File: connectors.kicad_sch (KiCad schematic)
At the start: 24 parts, among them J1 Conn_01x02, J4 USB_C_Receptacle_USB2.0_14P, M1 Motor_Servo, M2 Motor_Servo, Q1 Q_NMOS, Q2 Q_NMOS, U5 LM74502

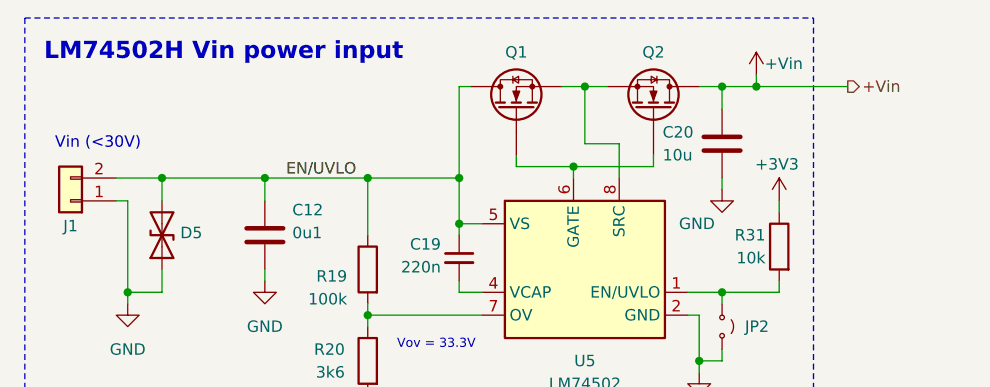
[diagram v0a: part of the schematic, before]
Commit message: schem: add test points
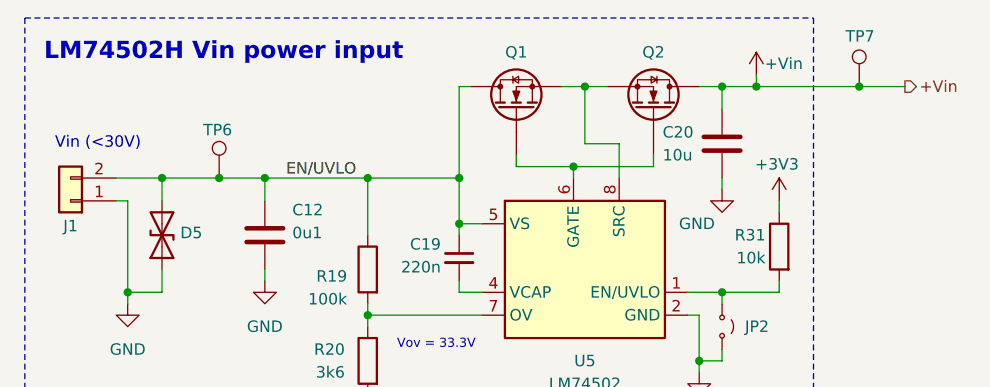
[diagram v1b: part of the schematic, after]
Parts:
- added TP6, TP7: TestPoint, symbol Connector:TestPoint
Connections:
- net +Vin: now also TP7.1
- net EN/UVLO: now also TP6.1
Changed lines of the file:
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@@
 	)
 	(junction
+		(at 240.03 85.09)
+		(diameter 0)
+		(color 0 0 0 0)
+	)
+	(junction
 		(at 93.98 147.32)
 		(diameter 0)
@@
 	)
 	(junction
+		(at 168.91 95.25)
+		(diameter 0)
+		(color 0 0 0 0)
+	)
+	(junction
 		(at 93.98 157.48)
 		(diameter 0)
@@
 	(wire
 		(pts
+			(xy 240.03 85.09) (xy 245.11 85.09)
+		)
+		(stroke
+			(width 0)
+			(type default)
+		)
+	)
+	(wire
+		(pts
 			(xy 162.56 107.95) (xy 158.75 107.95)
 		)
@@
 	(wire
 		(pts
-			(xy 162.56 95.25) (xy 173.99 95.25)
+			(xy 162.56 95.25) (xy 168.91 95.25)
 		)
 		(stroke
@@
 	(wire
 		(pts
-			(xy 228.6 85.09) (xy 238.76 85.09)
+			(xy 228.6 85.09) (xy 240.03 85.09)
 		)
 		(stroke
@@
 	(wire
 		(pts
+			(xy 168.91 95.25) (xy 173.99 95.25)
+		)
+		(stroke
+			(width 0)
+			(type default)
+		)
+	)
+	(wire
+		(pts
 			(xy 90.17 106.68) (xy 87.63 106.68)
 		)
@@
 	(hierarchical_label "+Vin"
 		(shape output)
-		(at 238.76 85.09 0)
+		(at 245.11 85.09 0)
 		(effects
 			(font
@@
 	)
 	(symbol
+		(lib_id "Connector:TestPoint")
+		(at 240.03 85.09 0)
+		(unit 1)
+		(exclude_from_sim no)
+		(in_bom yes)
+		(on_board yes)
+		(dnp no)
+		(property "Reference" "TP7"
+			(at 238.506 79.502 0)
+			(effects
+				(font
+					(size 1.27 1.27)
+				)
+				(justify left)
+			)
+		)
+		(property "Value" "TestPoint"
+			(at 242.57 83.0579 0)
+			(effects
+				(font
+					(size 1.27 1.27)
+				)
+				(justify left)
+				(hide yes)
+			)
+		)
+		(property "Footprint" ""
+			(at 245.11 85.09 0)
+			(effects
+				(font
+					(size 1.27 1.27)
+				)
+				(hide yes)
+			)
+		)
+		(property "Datasheet" "~"
+			(at 245.11 85.09 0)
+			(effects
+				(font
+					(size 1.27 1.27)
+				)
+				(hide yes)
+			)
+		)
+		(property "Description" "test point"
+			(at 240.03 85.09 0)
+			(effects
+				(font
+					(size 1.27 1.27)
+				)
+				(hide yes)
+			)
+		)
+		(pin "1"
+		)
+		(instances
+			(project "motor-power-poc"
+				(path "/a1dc4c9e-7b20-4b66-a693-9133bc644c6b/dba74ea3-505d-49e4-ba26-48f567962081"
+					(reference "TP7")
+					(unit 1)
+				)
+			)
+		)
+	)
+	(symbol
 		(lib_id "power:+3V3")
 		(at 231.14 97.79 0)
@@
 					(unit 1)
 				)
+			)
+		)
+	)
+	(symbol
+		(lib_id "Connector:TestPoint")
+		(at 168.91 95.25 0)
+		(unit 1)
+		(exclude_from_sim no)
+		(in_bom yes)
+		(on_board yes)
+		(dnp no)
+		(property "Reference" "TP6"
+			(at 167.132 89.916 0)
+			(effects
+				(font
+					(size 1.27 1.27)
+				)
+				(justify left)
+			)
+		)
+		(property "Value" "TestPoint"
+			(at 171.45 93.2179 0)
+			(effects
+				(font
+					(size 1.27 1.27)
+				)
+				(justify left)
+				(hide yes)
+			)
+		)
+		(property "Footprint" ""
+			(at 173.99 95.25 0)
+			(effects
+				(font
+					(size 1.27 1.27)
+				)
+				(hide yes)
+			)
+		)
+		(property "Datasheet" "~"
+			(at 173.99 95.25 0)
+			(effects
+				(font
+					(size 1.27 1.27)
+				)
+				(hide yes)
+			)
+		)
+		(property "Description" "test point"
+			(at 168.91 95.25 0)
+			(effects
+				(font
+					(size 1.27 1.27)
+				)
+				(hide yes)
+			)
+		)
+		(pin "1"
+		)
+		(instances
+			(project "motor-power-poc"
+				(path "/a1dc4c9e-7b20-4b66-a693-9133bc644c6b/dba74ea3-505d-49e4-ba26-48f567962081"
+					(reference "TP6")
+					(unit 1)
+				)

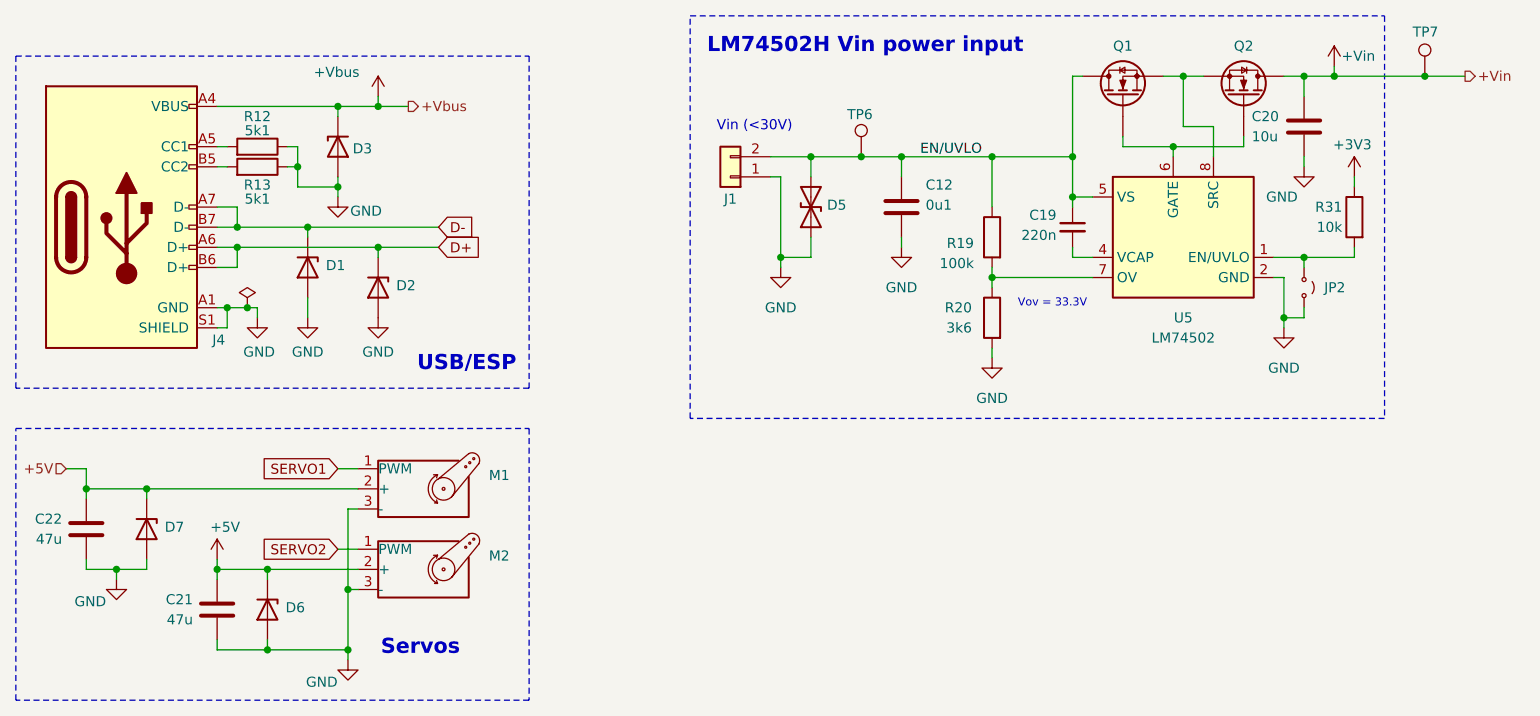
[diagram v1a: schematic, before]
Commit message: schem: renumber
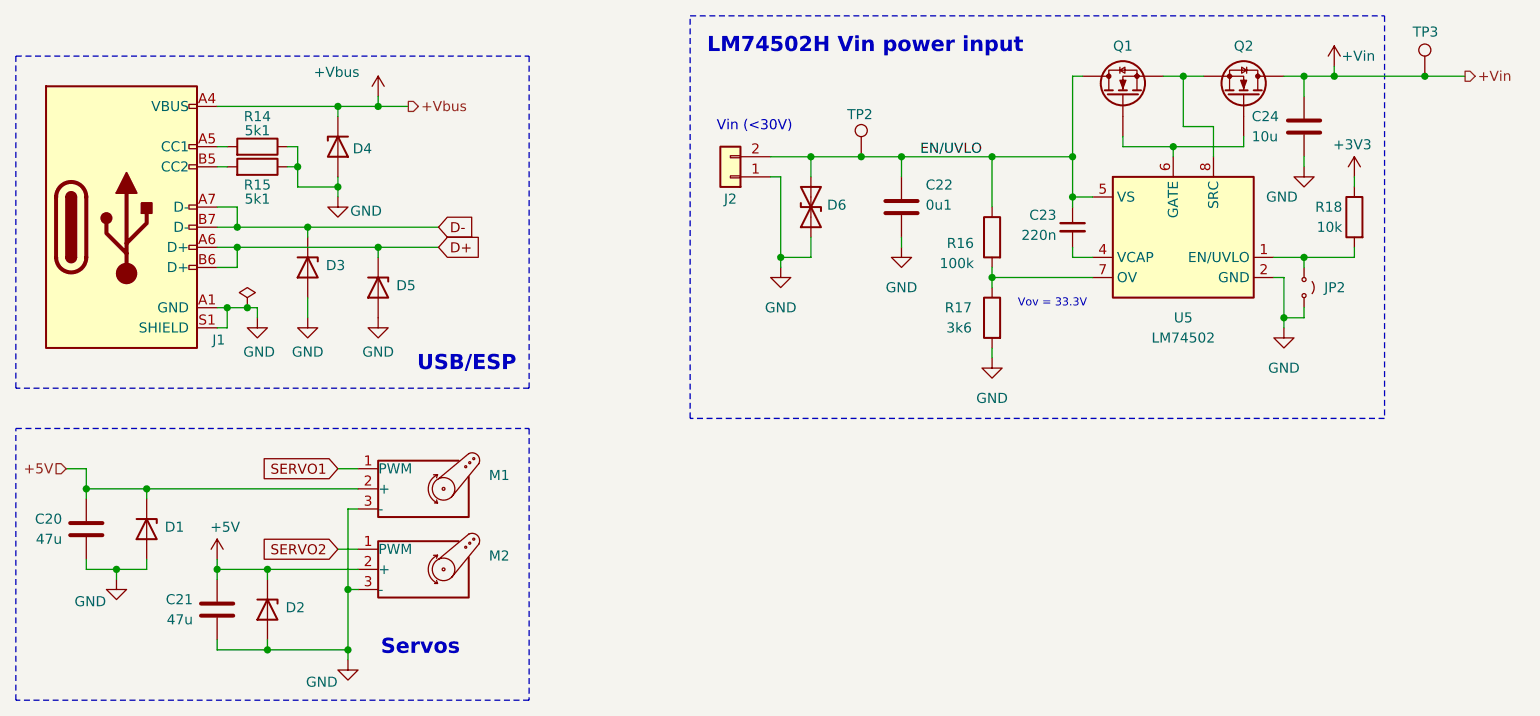
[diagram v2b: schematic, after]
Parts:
- renumbered C22 to C20, C12 to C22, C19 to C23, C20 to C24, D7 to D1, D6 to D2, D1 to D3, D3 to D4, D2 to D5, D5 to D6, J4 to J1, J1 to J2, R12 to R14, R13 to R15, R19 to R16, R20 to R17, R31 to R18, TP6 to TP2, TP7 to TP3

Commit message: schem: run and fix ERC
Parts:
- U5: footprint GLCS:SOT-23-8 -> GLCS:SOT-23-THIN-8
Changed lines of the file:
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@@
 	)
 	(junction
+		(at 232.41 85.09)
+		(diameter 0)
+		(color 0 0 0 0)
+	)
+	(junction
 		(at 240.03 85.09)
 		(diameter 0)
@@
 		(color 0 0 0 0)
 	)
+	(junction
+		(at 165.1 95.25)
+		(diameter 0)
+		(color 0 0 0 0)
+	)
 	(wire
 		(pts
@@
 	(wire
 		(pts
+			(xy 232.41 85.09) (xy 240.03 85.09)
+		)
+		(stroke
+			(width 0)
+			(type default)
+		)
+	)
+	(wire
+		(pts
 			(xy 90.17 106.68) (xy 107.95 106.68)
 		)
@@
 	(wire
 		(pts
+			(xy 165.1 95.25) (xy 168.91 95.25)
+		)
+		(stroke
+			(width 0)
+			(type default)
+		)
+	)
+	(wire
+		(pts
 			(xy 102.87 100.33) (xy 102.87 99.06)
 		)
@@
 	(wire
 		(pts
-			(xy 162.56 95.25) (xy 168.91 95.25)
+			(xy 162.56 95.25) (xy 165.1 95.25)
 		)
 		(stroke
@@
 	(wire
 		(pts
-			(xy 228.6 85.09) (xy 240.03 85.09)
+			(xy 228.6 85.09) (xy 232.41 85.09)
 		)
 		(stroke
@@
 	)
 	(symbol
+		(lib_id "power:PWR_FLAG")
+		(at 232.41 85.09 180)
+		(unit 1)
+		(exclude_from_sim no)
+		(in_bom yes)
+		(on_board yes)
+		(dnp no)
+		(fields_autoplaced yes)
+		(property "Reference" "#FLG07"
+			(at 232.41 86.995 0)
+			(effects
+				(font
+					(size 1.27 1.27)
+				)
+				(hide yes)
+			)
+		)
+		(property "Value" "PWR_FLAG"
+			(at 232.41 90.17 0)
+			(effects
+				(font
+					(size 1.27 1.27)
+				)
+				(hide yes)
+			)
+		)
+		(property "Footprint" ""
+			(at 232.41 85.09 0)
+			(effects
+				(font
+					(size 1.27 1.27)
+				)
+				(hide yes)
+			)
+		)
+		(property "Datasheet" "~"
+			(at 232.41 85.09 0)
+			(effects
+				(font
+					(size 1.27 1.27)
+				)
+				(hide yes)
+			)
+		)
+		(property "Description" "Special symbol for telling ERC where power comes from"
+			(at 232.41 85.09 0)
+			(effects
+				(font
+					(size 1.27 1.27)
+				)
+				(hide yes)
+			)
+		)
+		(pin "1"
+		)
+		(instances
+			(project "motor-power-poc"
+				(path "/a1dc4c9e-7b20-4b66-a693-9133bc644c6b/dba74ea3-505d-49e4-ba26-48f567962081"
+					(reference "#FLG07")
+					(unit 1)
+				)
+			)
+		)
+	)
+	(symbol
 		(lib_id "Device:D_TVS")
 		(at 162.56 101.6 90)
@@
 	)
 	(symbol
+		(lib_id "power:PWR_FLAG")
+		(at 165.1 95.25 0)
+		(unit 1)
+		(exclude_from_sim no)
+		(in_bom yes)
+		(on_board yes)
+		(dnp no)
+		(fields_autoplaced yes)
+		(property "Reference" "#FLG06"
+			(at 165.1 93.345 0)
+			(effects
+				(font
+					(size 1.27 1.27)
+				)
+				(hide yes)
+			)
+		)
+		(property "Value" "PWR_FLAG"
+			(at 165.1 90.17 0)
+			(effects
+				(font
+					(size 1.27 1.27)
+				)
+				(hide yes)
+			)
+		)
+		(property "Footprint" ""
+			(at 165.1 95.25 0)
+			(effects
+				(font
+					(size 1.27 1.27)
+				)
+				(hide yes)
+			)
+		)
+		(property "Datasheet" "~"
+			(at 165.1 95.25 0)
+			(effects
+				(font
+					(size 1.27 1.27)
+				)
+				(hide yes)
+			)
+		)
+		(property "Description" "Special symbol for telling ERC where power comes from"
+			(at 165.1 95.25 0)
+			(effects
+				(font
+					(size 1.27 1.27)
+				)
+				(hide yes)
+			)
+		)
+		(pin "1"
+		)
+		(instances
+			(project "motor-power-poc"
+				(path "/a1dc4c9e-7b20-4b66-a693-9133bc644c6b/dba74ea3-505d-49e4-ba26-48f567962081"
+					(reference "#FLG06")
+					(unit 1)
+				)
+			)
+		)
+	)
+	(symbol
 		(lib_id "power:GND")
 		(at 102.87 100.33 0)
@@
 			)
 		)
-		(property "Footprint" "GLCS:SOT-23-8"
+		(property "Footprint" "GLCS:SOT-23-THIN-8"
 			(at 200.025 114.3 0)
 			(effects

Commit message: schem: add title
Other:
- company: (none) -> Rémi Ait-Younes
- title: (none) -> Motor Power POC
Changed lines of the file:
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@@
 	(generator_version "9.0")
 	(paper "A4")
+	(title_block
+		(title "Motor Power POC")
+		(date "2025-11-30")
+		(rev "01")
+		(company "Rémi Ait-Younes")
+	)
 	(rectangle
 		(start 147.32 77.47)

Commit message: schem: assign footprints
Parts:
- C20, C21: footprint (none) -> Capacitor_SMD:C_1206_3216Metric
- C22, C23: footprint (none) -> Capacitor_SMD:C_0402_1005Metric
- C24: footprint (none) -> Capacitor_SMD:C_0805_2012Metric
- D1, D2, D3, D5: footprint Pers:Diode_DFN1006 -> GLCS:Diode_DFN1006; symbol Pers:H5VU10U -> GLCS:H5VU10U
- D4: footprint Diode_SMD:D_SMB -> GLCS:Diode_DFN1006; symbol Pers:H5VU10U -> GLCS:H5VU10U
- D6: footprint (none) -> Diode_SMD:D_SMB; Basic (none) -> E; JLCPCB Part # (none) -> C2925441; Manufacturer (none) -> Liown; Manufacturer Part Number (none) -> SMBJ30CA
- JP2: footprint (none) -> Connector_PinHeader_2.54mm:PinHeader_1x02_P2.54mm_Vertical
- M1, M2: footprint (none) -> Connector_PinHeader_2.54mm:PinHeader_1x03_P2.54mm_Vertical
- Q1, Q2: footprint (none) -> Package_SO:Vishay_PowerPAK_1212-8_Single
- R16, R18: footprint (none) -> Resistor_SMD:R_0402_1005Metric
- R17: footprint (none) -> Resistor_SMD:R_0603_1608Metric
- TP2, TP3: footprint (none) -> GLCS:TestPoint_Keystone_5015_Micro_Mini
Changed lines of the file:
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@@
 			)
 		)
-		(property "Footprint" ""
+		(property "Footprint" "Diode_SMD:D_SMB"
 			(at 162.56 101.6 0)
 			(effects
@@
 		(property "Description" "Bidirectional transient-voltage-suppression diode"
 			(at 162.56 101.6 0)
+			(effects
+				(font
+					(size 1.27 1.27)
+				)
+				(hide yes)
+			)
+		)
+		(property "Basic" "E"
+			(at 162.56 101.6 90)
+			(effects
+				(font
+					(size 1.27 1.27)
+				)
+				(hide yes)
+			)
+		)
+		(property "JLCPCB Part #" "C2925441"
+			(at 162.56 101.6 90)
+			(effects
+				(font
+					(size 1.27 1.27)
+				)
+				(hide yes)
+			)
+		)
+		(property "Manufacturer" "Liown"
+			(at 162.56 101.6 90)
+			(effects
+				(font
+					(size 1.27 1.27)
+				)
+				(hide yes)
+			)
+		)
+		(property "Manufacturer Part Number" "SMBJ30CA"
+			(at 162.56 101.6 90)
 			(effects
 				(font
@@
 			)
 		)
-		(property "Footprint" ""
+		(property "Footprint" "Capacitor_SMD:C_1206_3216Metric"
 			(at 70.1548 146.05 0)
 			(effects
@@
 	)
 	(symbol
-		(lib_id "Pers:H5VU10U")
+		(lib_id "GLCS:H5VU10U")
 		(at 107.95 111.76 270)
 		(unit 1)
@@
 			)
 		)
-		(property "Footprint" "Pers:Diode_DFN1006"
+		(property "Footprint" "GLCS:Diode_DFN1006"
 			(at 103.505 111.76 0)
 			(effects
@@
 	)
 	(symbol
-		(lib_id "Pers:H5VU10U")
+		(lib_id "GLCS:H5VU10U")
 		(at 99.06 109.22 270)
 		(unit 1)
@@
 			)
 		)
-		(property "Footprint" "Pers:Diode_DFN1006"
+		(property "Footprint" "GLCS:Diode_DFN1006"
 			(at 94.615 109.22 0)
 			(effects
@@
 			)
 		)
-		(property "Footprint" ""
+		(property "Footprint" "Connector_PinHeader_2.54mm:PinHeader_1x02_P2.54mm_Vertical"
 			(at 224.79 111.76 0)
 			(effects
@@
 			)
 		)
-		(property "Footprint" ""
+		(property "Footprint" "Package_SO:Vishay_PowerPAK_1212-8_Single"
 			(at 219.71 82.55 0)
 			(effects
@@
 	)
 	(symbol
-		(lib_id "Pers:H5VU10U")
+		(lib_id "GLCS:H5VU10U")
 		(at 78.74 142.24 270)
 		(unit 1)
@@
 			)
 		)
-		(property "Footprint" "Pers:Diode_DFN1006"
+		(property "Footprint" "GLCS:Diode_DFN1006"
 			(at 74.295 142.24 0)
 			(effects
@@
 			)
 		)
-		(property "Footprint" ""
+		(property "Footprint" "Capacitor_SMD:C_0402_1005Metric"
 			(at 195.58 104.14 0)
 			(effects
@@
 			)
 		)
-		(property "Footprint" ""
+		(property "Footprint" "Capacitor_SMD:C_0402_1005Metric"
 			(at 173.0248 105.41 0)
 			(effects
@@
 			)
 		)
-		(property "Footprint" ""
+		(property "Footprint" "GLCS:TestPoint_Keystone_5015_Micro_Mini"
 			(at 245.11 85.09 0)
 			(effects
@@
 			)
 		)
-		(property "Footprint" ""
+		(property "Footprint" "GLCS:TestPoint_Keystone_5015_Micro_Mini"
 			(at 173.99 95.25 0)
 			(effects
@@
 			)
 		)
-		(property "Footprint" ""
+		(property "Footprint" "Capacitor_SMD:C_0805_2012Metric"
 			(at 223.8248 95.25 0)
 			(effects
@@
 	)
 	(symbol
-		(lib_id "Pers:H5VU10U")
+		(lib_id "GLCS:H5VU10U")
 		(at 102.87 93.98 90)
 		(mirror x)
@@
 			)
 		)
-		(property "Footprint" "Diode_SMD:D_SMB"
+		(property "Footprint" "GLCS:Diode_DFN1006"
 			(at 107.315 93.98 0)
 			(effects
@@
 			)
 		)
-		(property "Datasheet" "https://www.lcsc.com/datasheet/C78395.pdf"
+		(property "Datasheet" "https://datasheet.lcsc.com/lcsc/2504101957_hongjiacheng-H5VU10U_C22395519.pdf"
 			(at 102.87 93.98 0)
 			(effects
@@
 			)
 		)
-		(property "Description" "10.5V 1uA 5.8V 58.1A 6.45V 600W Bidirectional TVS SMB(DO-214AA) ESD and Surge Protection (TVS/ESD) ROHS"
+		(property "Description" "-55℃~+155℃ 0.8pF 16V 200nA 55W@8/20us 5A@8/20us 5V 6V ESD IEC 61000-4-2 Unidirectional DFN1006-2L ESD and Surge Protection (TVS/ESD) ROHS"
 			(at 102.87 93.98 0)
 			(effects
@@
 			)
 		)
-		(property "Footprint" ""
+		(property "Footprint" "Resistor_SMD:R_0603_1608Metric"
 			(at 187.198 115.57 90)
 			(effects
@@
 			)
 		)
-		(property "Footprint" ""
+		(property "Footprint" "Capacitor_SMD:C_1206_3216Metric"
 			(at 86.6648 156.21 0)
 			(effects
@@
 	)
 	(symbol
-		(lib_id "Pers:H5VU10U")
+		(lib_id "GLCS:H5VU10U")
 		(at 93.98 152.4 270)
 		(unit 1)
@@
 			)
 		)
-		(property "Footprint" "Pers:Diode_DFN1006"
+		(property "Footprint" "GLCS:Diode_DFN1006"
 			(at 89.535 152.4 0)
 			(effects
@@
 			)
 		)
-		(property "Footprint" ""
+		(property "Footprint" "Connector_PinHeader_2.54mm:PinHeader_1x03_P2.54mm_Vertical"
 			(at 113.03 152.146 0)
 			(effects
@@
 			)
 		)
-		(property "Footprint" ""
+		(property "Footprint" "Connector_PinHeader_2.54mm:PinHeader_1x03_P2.54mm_Vertical"
 			(at 113.03 141.986 0)
 			(effects
@@
 			)
 		)
-		(property "Footprint" ""
+		(property "Footprint" "Resistor_SMD:R_0402_1005Metric"
 			(at 187.198 105.41 90)
 			(effects
@@
 			)
 		)
-		(property "Footprint" ""
+		(property "Footprint" "Package_SO:Vishay_PowerPAK_1212-8_Single"
 			(at 199.39 82.55 0)
 			(effects
@@
 			)
 		)
-		(property "Footprint" ""
+		(property "Footprint" "Resistor_SMD:R_0402_1005Metric"
 			(at 232.918 102.87 90)
 			(effects

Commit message: schem: add connectors footprint
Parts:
- J2: footprint (none) -> TerminalBlock_Phoenix:TerminalBlock_Phoenix_MKDS-1,5-2-5.08_1x02_P5.08mm_Horizontal
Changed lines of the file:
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@@
 			)
 		)
-		(property "Footprint" ""
+		(property "Footprint" "TerminalBlock_Phoenix:TerminalBlock_Phoenix_MKDS-1,5-2-5.08_1x02_P5.08mm_Horizontal"
 			(at 152.4 97.79 0)
 			(effects

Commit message: schem: add ordering info to BOM
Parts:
- C20, C21: Basic (none) -> Y; JLCPCB Part # (none) -> C96123; Manufacturer (none) -> Samsung Electro-Mechanics; Manufacturer Part Number (none) -> CL31A476MPHNNNE
- C22: Basic (none) -> Y; JLCPCB Part # (none) -> C307331; Manufacturer (none) -> Samsung Electro-Mechanics; Manufacturer Part Number (none) -> CL05B104KB54PNC
- C23: Basic (none) -> Y; JLCPCB Part # (none) -> C16772; Manufacturer (none) -> Samsung Electro-Mechanics; Manufacturer Part Number (none) -> CL05B224KO5NNNC
- C24: Basic (none) -> Y; JLCPCB Part # (none) -> C440198; Manufacturer (none) -> Murata; Manufacturer Part Number (none) -> GRM21BR61H106KE43L
- J2, JP2, M1, M2: now left out of the parts list
- Q1, Q2: Basic (none) -> X; JLCPCB Part # (none) -> C111309; Manufacturer (none) -> Vishay Intertech; Manufacturer Part Number (none) -> SIS412DN-T1-GE3
- R16: Basic (none) -> Y; JLCPCB Part # (none) -> C25741; Manufacturer (none) -> Uniroyal Elec; Manufacturer Part Number (none) -> 0402WGF1003TCE
- R17: Basic (none) -> Y; JLCPCB Part # (none) -> C22980; Manufacturer (none) -> Uniroyal Elec; Manufacturer Part Number (none) -> 0603WAF3601T5E
- R18: Basic (none) -> Y; JLCPCB Part # (none) -> C25744; Manufacturer (none) -> Uniroyal Elec; Manufacturer Part Number (none) -> 0402WGF1002TCE
- TP2, TP3: Basic (none) -> X; JLCPCB Part # (none) -> C2906768; Manufacturer (none) -> Keystone; Manufacturer Part Number (none) -> 5015
- U5: Basic (none) -> X; JLCPCB Part # (none) -> C3236215; Manufacturer (none) -> Texas Instruments; Manufacturer Part Number (none) -> LM74502DDFR
